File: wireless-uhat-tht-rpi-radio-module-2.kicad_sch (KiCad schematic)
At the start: 17 parts, among them J1 GPIO, J2 DEBUG, U1 CAT24C256_EP

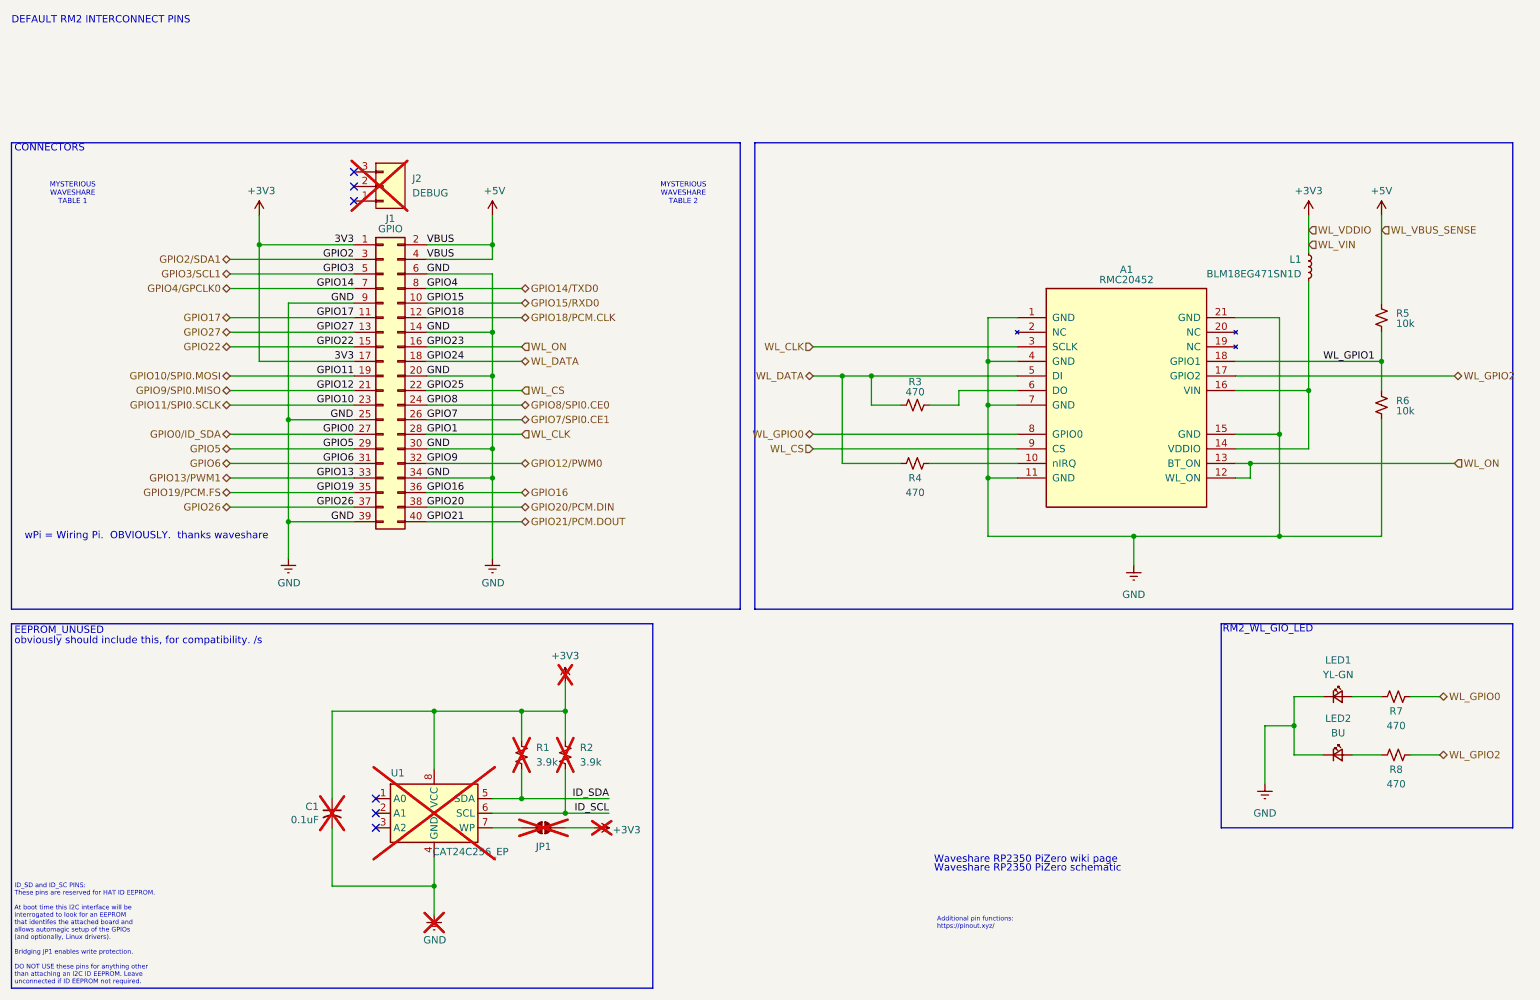
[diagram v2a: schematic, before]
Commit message: tl;dr: added fonts, moved RM2 module, switched to CC by-SA 4.0 license
=======================================================================
added:
  ./
      LICENSE - switched to CC by-SA license
  .kinotes/
      wireless-uhat-tht-rpi-radio-module-2_worklog_20260220.md - am i
        supposed to be writing in this?  whoops

-----------------------------------------------------------------------
removed:
  ./
      fp-info-cache - finally remembered to untrack
      wireless-uhat-tht-rpi-radio-module-2.kicad_prl - same

-----------------------------------------------------------------------
modified:
  ./
      wireless-uhat-tht-rpi-radio-module-2.kicad_pcb - changed layout
        of board to move RM2 module safely within the board outline.  i
        haven't even gotten the 0.0.0 prototype yet so i hope i have to
        fix something else even more major later
      wireless-uhat-tht-rpi-radio-module-2.kicad_pro - rev -> 0.1.1 or
        something
      wireless-uhat-tht-rpi-radio-module-2.kicad_sch - removed eeprom
        section and debug connector

  .kinotes/
      settings.json - i should probably untrack this, who cares

  gerbers/
      wireless-uhat-tht-rpi-radio-module-2* - updated with fonts and new
        pcb layout

-----------------------------------------------------------------------
moved:
  ./wireless-uhat-tht-rpi-radio-module-2.kicad_* - rev 0.0.0
      -> r0-0-0/wireless-uhat-tht-rpi-radio-module-2.kicad_*

  .kinotes/KiNotes_wireless-uhat-rpi-radio-module-2.md
      -> r0-0-0/.kinotes/KiNotes_wireless-uhat-rpi-radio-module-2.md

  gerbers/wireless-uhat-tht-rpi-radio-module-2* - rev 0.0.0
      -> r0-0-0/gerbers/wireless-uhat-tht-rpi-radio-module-2*

  "but Cat, that's stupid? just use git version control FFS!"
      -> That is unfortunate.

-----------------------------------------------------------------------
renamed:
  .kinotes/KiNotes_wireless-uhat-rpi-radio-module-2.md
      -> .kinotes/KiNotes_wireless-uhat-tht-rpi-radio-module-2.m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
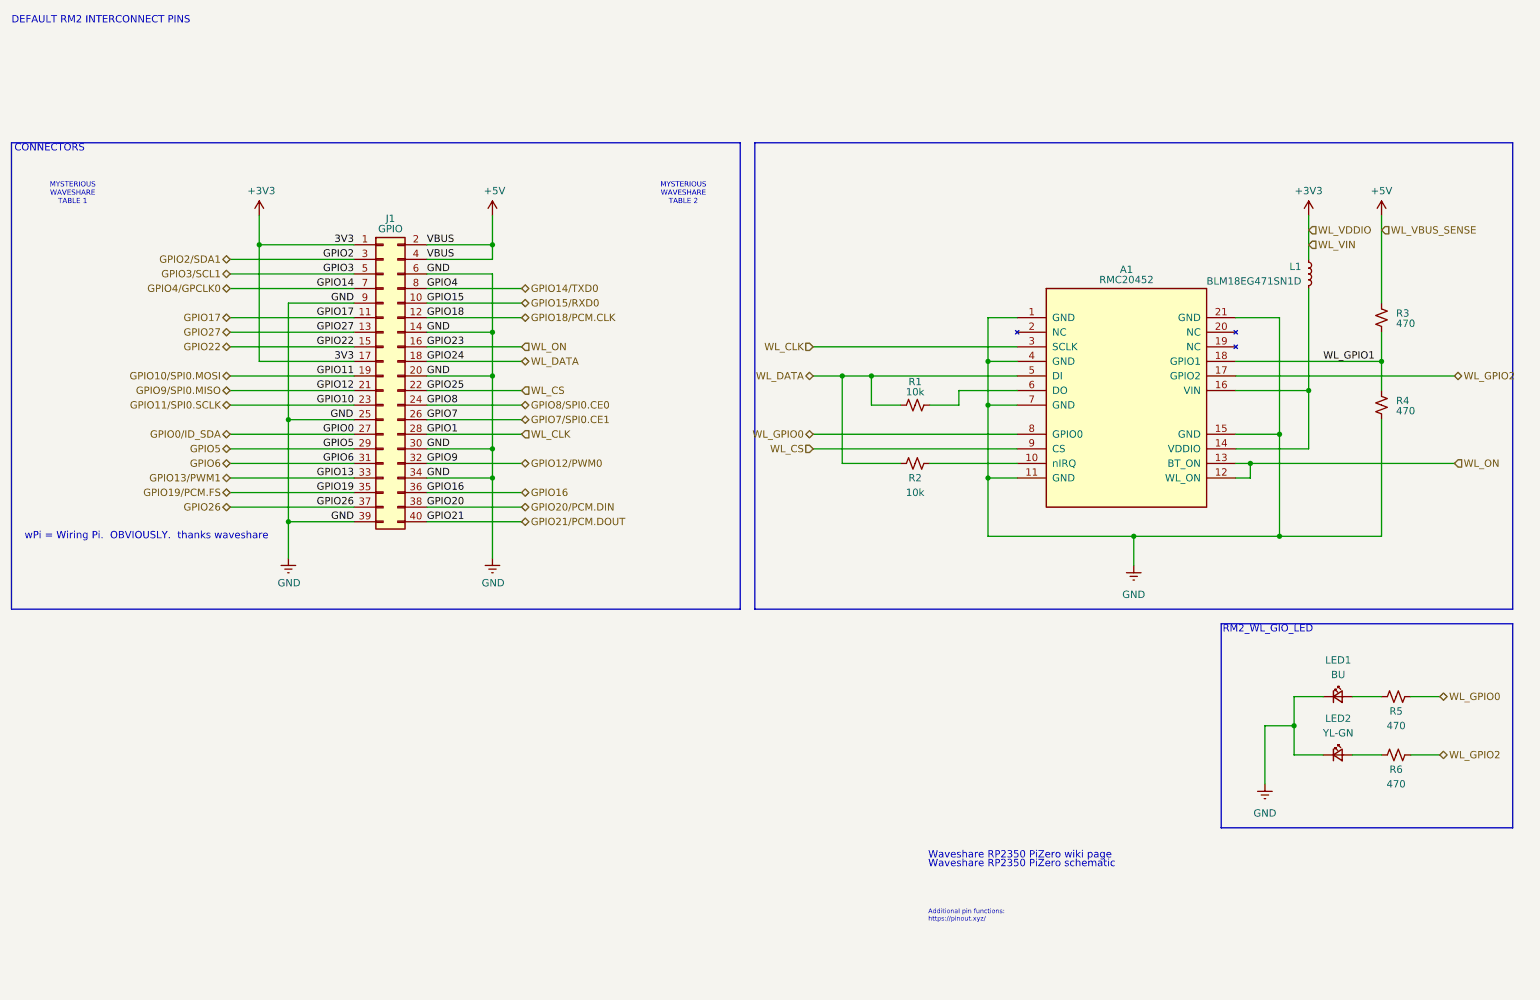
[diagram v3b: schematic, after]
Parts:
- removed C1: 0.1uF, Capacitor_SMD:C_0603_1608Metric_Pad1.08x0.95mm_HandSolder, symbol Device:C_Small_US
- removed J2: DEBUG, lsc-connector-board:BG12503A110440ND, symbol connectors-board-added:BG125-03-A-1-1-0440-N-D
- removed JP1: ID_WP, Jumper:SolderJumper-2_P1.3mm_Open_TrianglePad1.0x1.5mm, symbol Jumper:SolderJumper_2_Open
- removed R1, R2: 3.9k, Resistor_SMD:R_0805_2012Metric_Pad1.20x1.40mm_HandSolder, symbol Device:R_Small_US
- removed U1: CAT24C256_EP, Package_DFN_QFN:DFN-8-1EP_3x2mm_P0.5mm_EP1.3x1.5mm, symbol bad-symbol-edits:CAT24C256_EP
- A1: now in the parts list
- L1: Part Number BLM18EG471SN1D -> (none)
- LED1: value YL-GN -> BU; Height 0.9 -> 0.4; Manufacturer_Part_Number 599-0060-007F -> 599-0090-137F; Mouser Part Number 645-599-0060-007F -> (none); Mouser Price/Stock https://www.mouser.co.uk/ProductDetail/Dialight/599-0060-00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 -> (none); Part Number 599-0060-007F -> (none)
- LED2: value BU -> YL-GN; Height 0.4 -> 0.9; Manufacturer_Part_Number 599-0090-137F -> 599-0060-007F; Mouser Part Number (none) -> 645-599-0060-007F; Mouser Price/Stock (none) -> https://www.mouser.co.uk/ProductDetail/Dialight/599-0060-00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; Part Number 599-0090-137F -> (none)
- R1: renamed from R3; value 470 -> 10k; Part Number ERA-6AEB471V -> (none); part number (none) -> ERA-6AEB103V
- R2: renamed from R4; value 470 -> 10k; Part Number ERA-6AEB471V -> (none); part number (none) -> ERA-6AEB103V
- R3: renamed from R5; value 10k -> 470; Part Number ERA-6AEB103V -> (none); part number (none) -> ERA-6AEB471V
- R4: renamed from R6; value 10k -> 470; Part Number ERA-6AEB103V -> (none); part number (none) -> ERA-6AEB471V
- R5: renamed from R7; part number (none) -> ERA-6AEB471V
- R6: renamed from R8; Part Number ERA-6AEB471V -> (none); part number (none) -> ERA-6AEB471V
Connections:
- net EP renamed GND
- no-connect marks 6 -> 0
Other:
- note removed: "EEPROM_UNUSED"
- note removed: "ID_SD and ID_SC PINS: These pins are reserved for HAT ID EEPROM. At boot time this I2C interface will be interrogated to look for an EEPROM that identifes the attached board and allows automagic setup of the GPIOs (and optionally, Linux drivers). Bridging JP1 enables write protection. DO NOT USE these pins for anything other than attaching an I2C ID EEPROM. Leave unconnected if ID EEPROM not requ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"
- note removed: "obviously should include this, for compatibility. /s"
- company: (none) -> LiterallySomeCat
- title: (none) -> Radio Module 2 uHAT for Pico Series
- moved on the sheet: L1
